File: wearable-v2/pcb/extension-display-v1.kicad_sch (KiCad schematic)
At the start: 28 parts, among them J16 EA_WF030-39S, J17 JST_AUDIO_OUT, J18 DEBUG_HERALD, J19 FTDI_HERALD, J9 HERALD_V2_CONN_PLUG, U10 ATmega328PB-M, U13 TPA6139A2RGTR, U16 DRV2605LDGSR, U17 VG0832013D, U7 MX25R6435FZNIL0, Y2 8Mhz

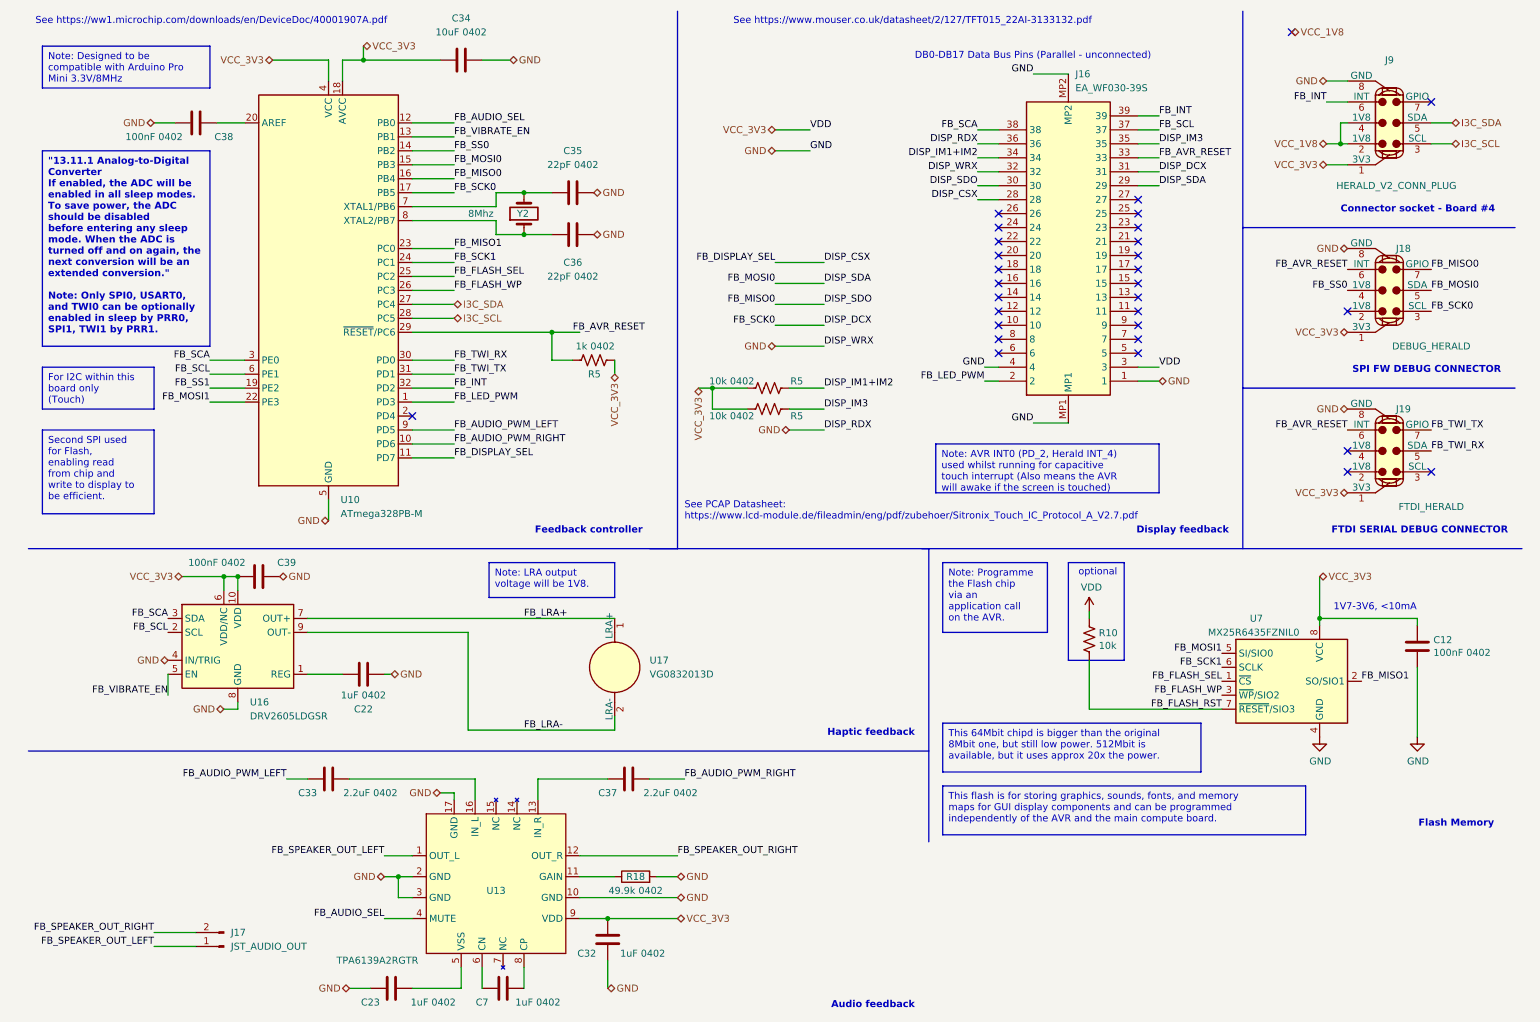
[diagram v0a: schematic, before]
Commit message: Added I2C and I3C notes and additional resistors
Signed-off-by: Adam Fowler <adam@adamfowler.org>
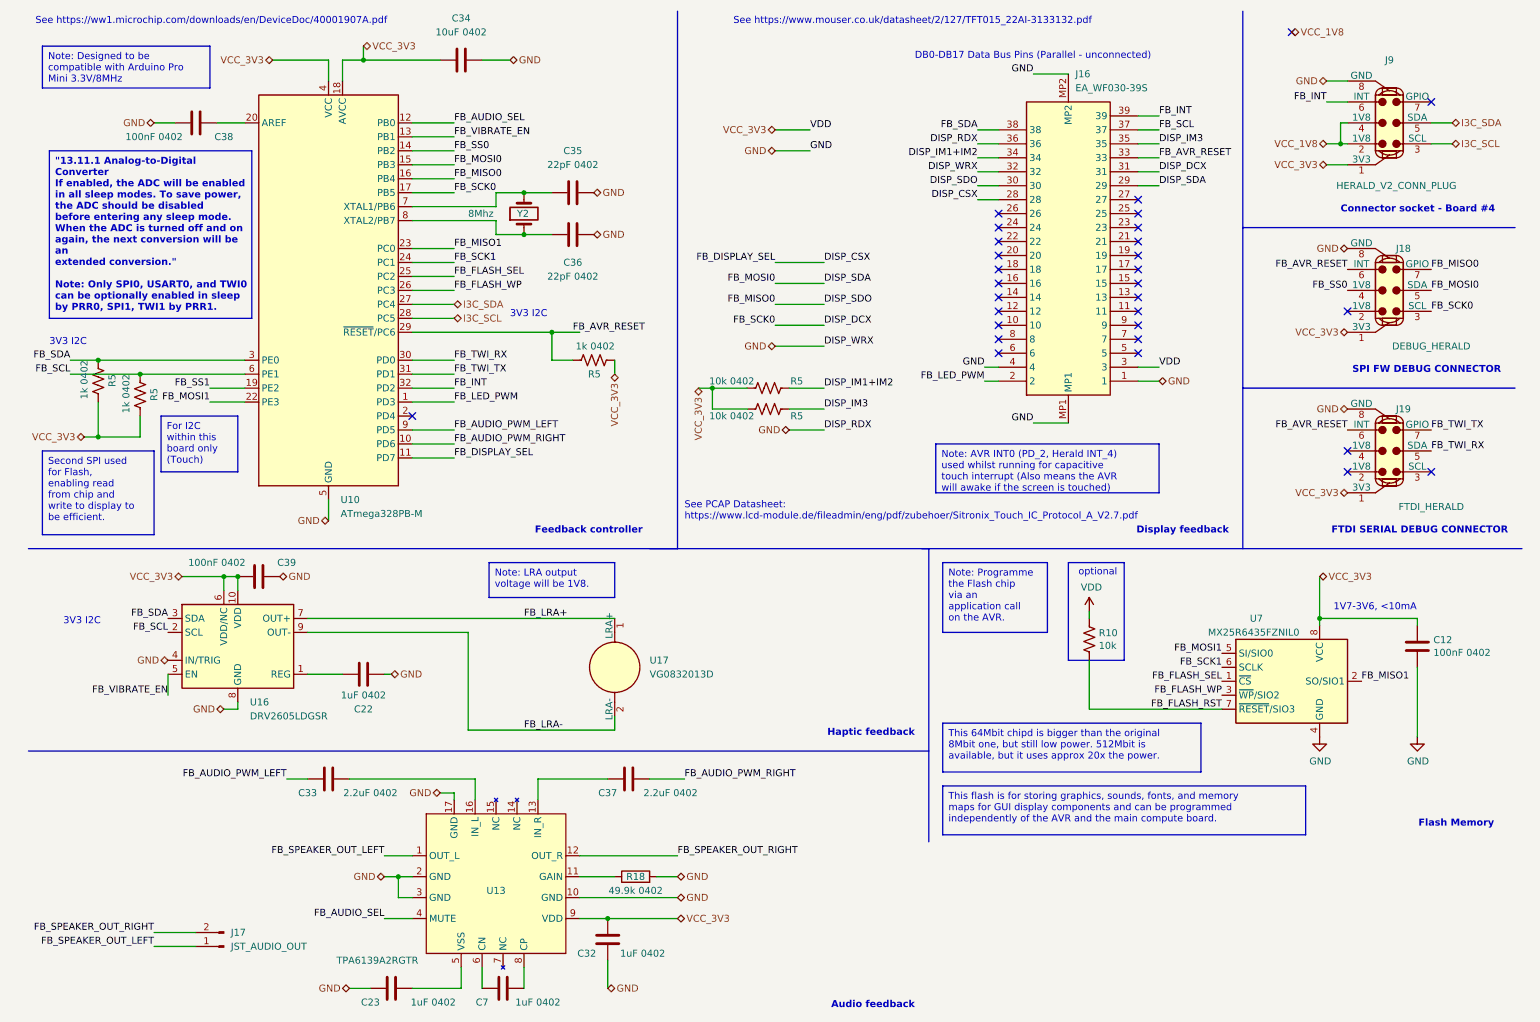
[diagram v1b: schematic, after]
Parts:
- added R5 (x2): 1k 0402, Resistor_SMD:R_0402_1005Metric, symbol Device:R_US
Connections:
- net FB_SCL: now also R5.2
- net VDD: now also R5.1, R5.1
- net FB_SCA renamed FB_SDA
- net FB_SDA: now also R5.2
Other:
- note added: "3V3 I2C"
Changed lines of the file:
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@@
   (junction (at 137.16 82.55) (diameter 0) (color 0 0 0 0)
   )
+  (junction (at 33.02 80.01) (diameter 0) (color 0 0 0 0)
+  )
   (junction (at 48.26 116.84) (diameter 0) (color 0 0 0 0)
   )
@@
   )
   (junction (at 50.8 116.84) (diameter 0) (color 0 0 0 0)
+  )
+  (junction (at 25.4 77.47) (diameter 0) (color 0 0 0 0)
+  )
+  (junction (at 25.4 91.44) (diameter 0) (color 0 0 0 0)
   )
   (no_connect (at 214.63 50.8))
@@
     (stroke (width 0) (type default))
   )
+  (wire (pts (xy 22.86 91.44) (xy 25.4 91.44))
+    (stroke (width 0) (type default))
+  )
   (wire (pts (xy 205.74 132.08) (xy 205.74 140.97))
     (stroke (width 0) (type default))
@@
     (stroke (width 0) (type default))
   )
+  (wire (pts (xy 25.4 85.09) (xy 25.4 91.44))
+    (stroke (width 0) (type default))
+  )
   (wire (pts (xy 148.59 67.31) (xy 157.48 67.31))
     (stroke (width 0) (type default))
@@
     (stroke (width 0) (type default))
   )
+  (wire (pts (xy 25.4 91.44) (xy 33.02 91.44))
+    (stroke (width 0) (type default))
+  )
   (wire (pts (xy 82.55 59.69) (xy 90.17 59.69))
     (stroke (width 0) (type default))
@@
     (stroke (width 0) (type default))
   )
-  (wire (pts (xy 45.72 80.01) (xy 52.07 80.01))
+  (wire (pts (xy 20.32 80.01) (xy 33.02 80.01))
     (stroke (width 0) (type default))
   )
@@
     (stroke (width 0) (type default))
   )
+  (wire (pts (xy 25.4 77.47) (xy 52.07 77.47))
+    (stroke (width 0) (type default))
+  )
   (wire (pts (xy 151.13 90.17) (xy 157.48 90.17))
     (stroke (width 0) (type default))
   )
+  (wire (pts (xy 33.02 87.63) (xy 33.02 91.44))
+    (stroke (width 0) (type default))
+  )
   (wire (pts (xy 137.16 82.55) (xy 143.51 82.55))
     (stroke (width 0) (type default))
@@
     (stroke (width 0) (type default))
   )
-  (wire (pts (xy 45.72 77.47) (xy 52.07 77.47))
+  (wire (pts (xy 20.32 77.47) (xy 25.4 77.47))
     (stroke (width 0) (type default))
   )
   (wire (pts (xy 105.41 153.67) (xy 118.11 153.67))
+    (stroke (width 0) (type default))
+  )
+  (wire (pts (xy 33.02 80.01) (xy 52.07 80.01))
     (stroke (width 0) (type default))
   )
@@
   )
   (text_box "\"13.11.1 Analog-to-Digital Converter\nIf enabled, the ADC will be enabled in all sleep modes. To save power, the ADC should be disabled\nbefore entering any sleep mode. When the ADC is turned off and on again, the next conversion will be an\nextended conversion.\"\n\nNote: Only SPI0, USART0, and TWI0 can be optionally enabled in sleep by PRR0, SPI1, TWI1 by PRR1."
-    (at 15.24 39.37 0) (size 30.48 35.56)
+    (at 16.51 39.37 0) (size 36.83 30.48)
     (stroke (width 0) (type default))
     (fill (type none))
@@
   )
   (text_box "Second SPI used for Flash, enabling read from chip and write to display to be efficient."
-    (at 15.24 90.17 0) (size 20.32 15.24)
+    (at 15.24 93.98 0) (size 20.32 15.24)
     (stroke (width 0) (type default))
     (fill (type none))
@@
   )
   (text_box "For I2C within this board only (Touch)"
-    (at 15.24 78.74 0) (size 20.32 7.62)
+    (at 36.83 87.63 0) (size 13.97 10.16)
     (stroke (width 0) (type default))
     (fill (type none))
@@
     (effects (font (size 1.27 1.27) bold) (justify right bottom))
   )
+  (text "3V3 I2C" (at 16.51 74.93 0)
+    (effects (font (size 1.27 1.27)) (justify left bottom))
+  )
   (text "Display feedback" (at 231.14 109.22 0)
     (effects (font (size 1.27 1.27) (thickness 0.254) bold) (justify right bottom))
@@
     (effects (font (size 1.27 1.27)) (justify left bottom))
   )
+  (text "3V3 I2C" (at 100.33 69.85 0)
+    (effects (font (size 1.27 1.27)) (justify left bottom))
+  )
   (text "See PCAP Datasheet: \nhttps://www.lcd-module.de/fileadmin/eng/pdf/zubehoer/Sitronix_Touch_IC_Protocol_A_V2.7.pdf"
     (at 132.08 106.68 0)
     (effects (font (size 1.27 1.27)) (justify left bottom))
   )
+  (text "3V3 I2C" (at 19.05 125.73 0)
+    (effects (font (size 1.27 1.27)) (justify left bottom))
+  )
   (label "VDD" (at 154.94 35.56 0) (fields_autoplaced)
     (effects (font (size 1.27 1.27)) (justify left bottom))
@@
     (effects (font (size 1.27 1.27)) (justify right bottom))
   )
-  (label "FB_SCL" (at 45.72 80.01 180) (fields_autoplaced)
+  (label "FB_SCL" (at 20.32 80.01 180) (fields_autoplaced)
     (effects (font (size 1.27 1.27)) (justify right bottom))
   )
@@
     (effects (font (size 1.27 1.27)) (justify right bottom))
   )
-  (label "FB_SCA" (at 38.1 124.46 180) (fields_autoplaced)
+  (label "FB_SDA" (at 38.1 124.46 180) (fields_autoplaced)
     (effects (font (size 1.27 1.27)) (justify right bottom))
   )
@@
     (effects (font (size 1.27 1.27)) (justify left bottom))
   )
-  (label "FB_SCA" (at 45.72 77.47 180) (fields_autoplaced)
+  (label "FB_SDA" (at 20.32 77.47 180) (fields_autoplaced)
     (effects (font (size 1.27 1.27)) (justify right bottom))
   )
@@
     (effects (font (size 1.27 1.27)) (justify left bottom))
   )
-  (label "FB_SCA" (at 185.42 35.56 180) (fields_autoplaced)
+  (label "FB_SDA" (at 185.42 35.56 180) (fields_autoplaced)
     (effects (font (size 1.27 1.27)) (justify right bottom))
   )
@@
   (hierarchical_label "GND" (shape bidirectional) (at 130.81 171.45 0) (fields_autoplaced)
     (effects (font (size 1.27 1.27)) (justify left))
+  )
+  (hierarchical_label "VCC_3V3" (shape bidirectional) (at 22.86 91.44 180) (fields_autoplaced)
+    (effects (font (size 1.27 1.27)) (justify right))
   )
   (hierarchical_label "GND" (shape bidirectional) (at 151.13 90.17 180) (fields_autoplaced)
@@
     )
   )
+  (symbol (lib_id "Device:R_US") (at 25.4 81.28 180) (unit 1)
+    (in_bom yes) (on_board yes) (dnp no)
+    (property "Reference" "R5" (at 27.94 80.01 90)
+      (effects (font (size 1.27 1.27)) (justify left))
+    )
+    (property "Value" "1k 0402" (at 22.86 77.47 90)
+      (effects (font (size 1.27 1.27)) (justify left))
+    )
+    (property "Footprint" "Resistor_SMD:R_0402_1005Metric" (at 24.384 81.026 90)
+      (effects (font (size 1.27 1.27)) hide)
+    )
+    (property "Datasheet" "~" (at 25.4 81.28 0)
+      (effects (font (size 1.27 1.27)) hide)
+    )
+    (property "Description" "Resistor, 1%, 63mW" (at 25.4 81.28 0)
+      (effects (font (size 1.27 1.27)) hide)
+    )
+    (property "MPN" "CRCW04021K00FKEDC" (at 25.4 81.28 0)
+      (effects (font (size 1.27 1.27)) hide)
+    )
+    (pin "1")
+    (pin "2")
+    (instances
+      (project "wearable-v2"
+        (path "/1eb7e8c9-86dc-4f6b-85aa-748b782af952/2bf2cd8a-43d3-474c-96a0-b76bc82af7f4"
+          (reference "R5") (unit 1)
+        )
+        (path "/1eb7e8c9-86dc-4f6b-85aa-748b782af952/b2450f58-45d3-4267-a96b-cde30ab720a0"
+          (reference "R21") (unit 1)
+        )
+      )
+      (project "wearable"
+        (path "/bdd943b2-035a-4beb-80ad-5c7e84260dde/00000000-0000-0000-0000-000060f1d377"
+          (reference "R24") (unit 1)
+        )
+      )
+    )
+  )
   (symbol (lib_id "Connector:Conn_01x02_Pin") (at 48.26 184.15 180) (unit 1)
     (in_bom yes) (on_board yes) (dnp no) (fields_autoplaced)
@@
         )
       )
+    )
+  )
+  (symbol (lib_id "Device:R_US") (at 33.02 83.82 180) (unit 1)
+    (in_bom yes) (on_board yes) (dnp no)
+    (property "Reference" "R5" (at 35.56 82.55 90)
+      (effects (font (size 1.27 1.27)) (justify left))
+    )
+    (property "Value" "1k 0402" (at 30.48 80.01 90)
+      (effects (font (size 1.27 1.27)) (justify left))
+    )
+    (property "Footprint" "Resistor_SMD:R_0402_1005Metric" (at 32.004 83.566 90)
+      (effects (font (size 1.27 1.27)) hide)
+    )
+    (property "Datasheet" "~" (at 33.02 83.82 0)
+      (effects (font (size 1.27 1.27)) hide)
+    )
+    (property "Description" "Resistor, 1%, 63mW" (at 33.02 83.82 0)
+      (effects (font (size 1.27 1.27)) hide)
+    )
+    (property "MPN" "CRCW04021K00FKEDC" (at 33.02 83.82 0)
+      (effects (font (size 1.27 1.27)) hide)
+    )
+    (pin "1")
+    (pin "2")
+    (instances
+      (project "wearable-v2"
+        (path "/1eb7e8c9-86dc-4f6b-85aa-748b782af952/2bf2cd8a-43d3-474c-96a0-b76bc82af7f4"
+          (reference "R5") (unit 1)
+        )
+        (path "/1eb7e8c9-86dc-4f6b-85aa-748b782af952/b2450f58-45d3-4267-a96b-cde30ab720a0"
+          (reference "R22") (unit 1)
+        )
+      )
+      (project "wearable"
+        (path "/bdd943b2-035a-4beb-80ad-5c7e84260dde/00000000-0000-0000-0000-000060f1d377"
+          (reference "R24") (unit 1)
+        )
+      )
